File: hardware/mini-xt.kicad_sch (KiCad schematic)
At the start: 0 parts

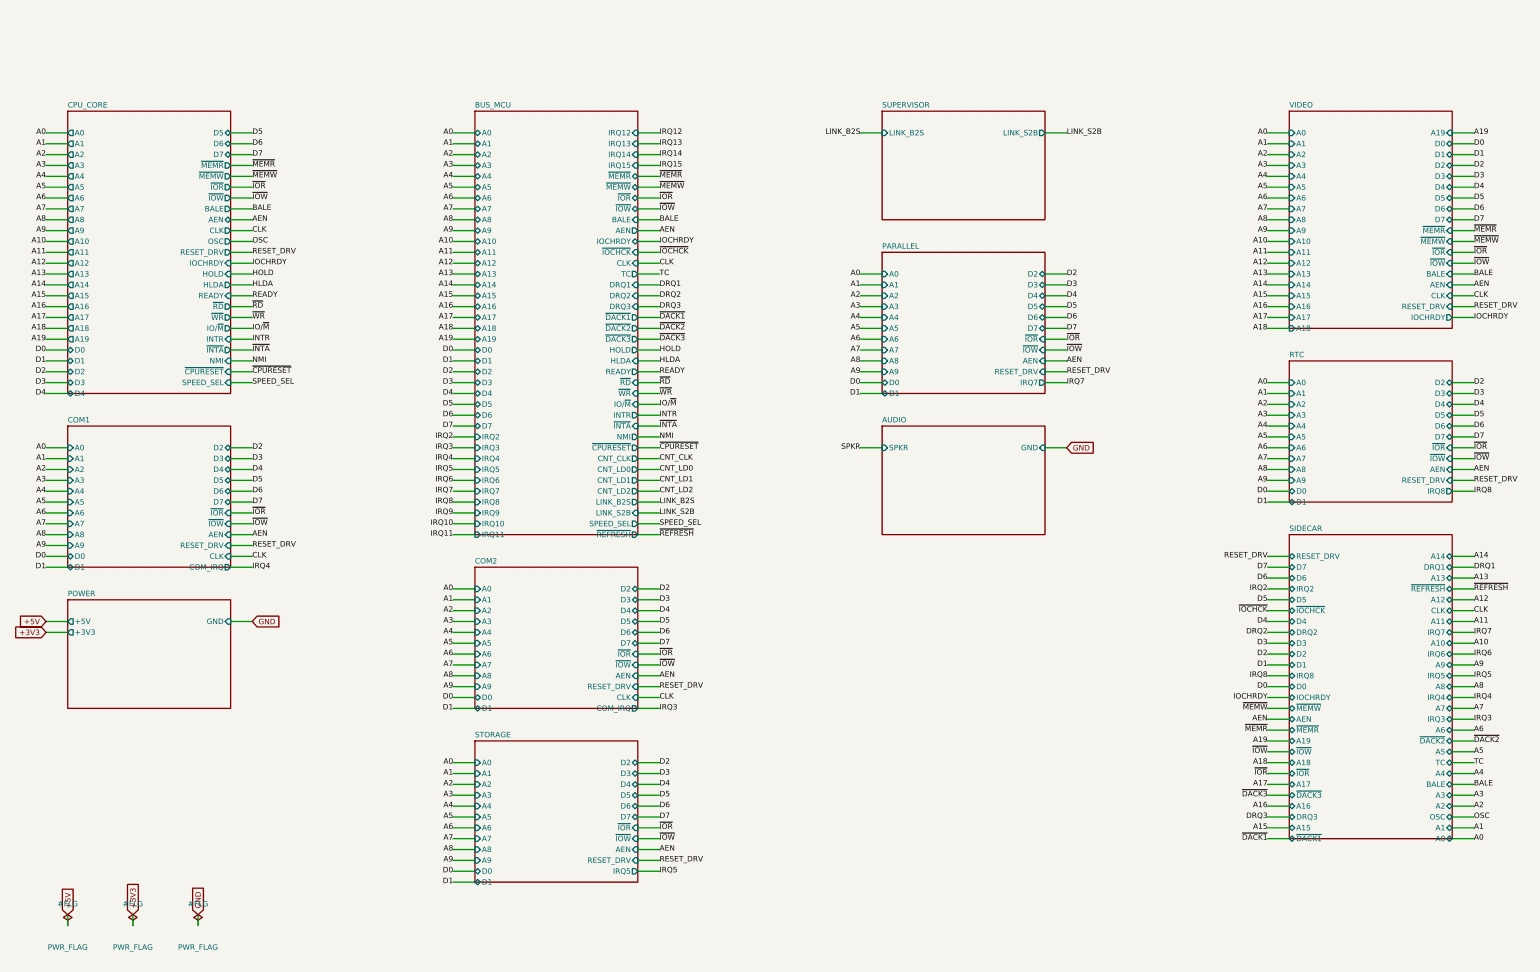
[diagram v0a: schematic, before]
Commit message: Fix all medium design-review findings (M1-M8)
- M1: Supervisor link moved to GPIO4/5 (real UART1 pair); POST -> GPIO6-15
- M2: CNT_RUN = LD0.LD1.LD2 gates every '163 CEP (load-cascade hazard)
- M3: ~WR / IO-M pruned to cpu_core-internal; DRQ2/3 pulled + noted;
  doc S5.2 "as built: 48/48" + S16 updated
- M4: true XT-IDE rev-2 map (A0<->A3 swap): data 0x300, latch 0x301,
  CS1 0x307/0x30F, drive DA0 = bus A3 - matches XTIDE UB "rev 2" type
- M5: COM4 -> bus IRQ2 line (IRQ9 via AT redirect); IRQ10/11/14/15 marked
  off-header; ~REFRESH added to mxbus ISA_CTRL; questions-sidecar superseded
- M6: card_isatest clock tree on unswitched V5RAW (spec S8)
- M7: card_isatest IRQ2-8/DRQ1-3 idle pull-downs (spec S4/S9)
- M8: com_port JP1 selects 16550 RX source (DB9 vs TTL console); 5V note

Rebuilt motherboard + cards; structural ERC = 0; netlist-verified.
Fix log in hardware/notes/design-review-2026-07-03.md (batch 3).

Co-Authored-By: Claude Fable 5 <noreply@anthropic.com>
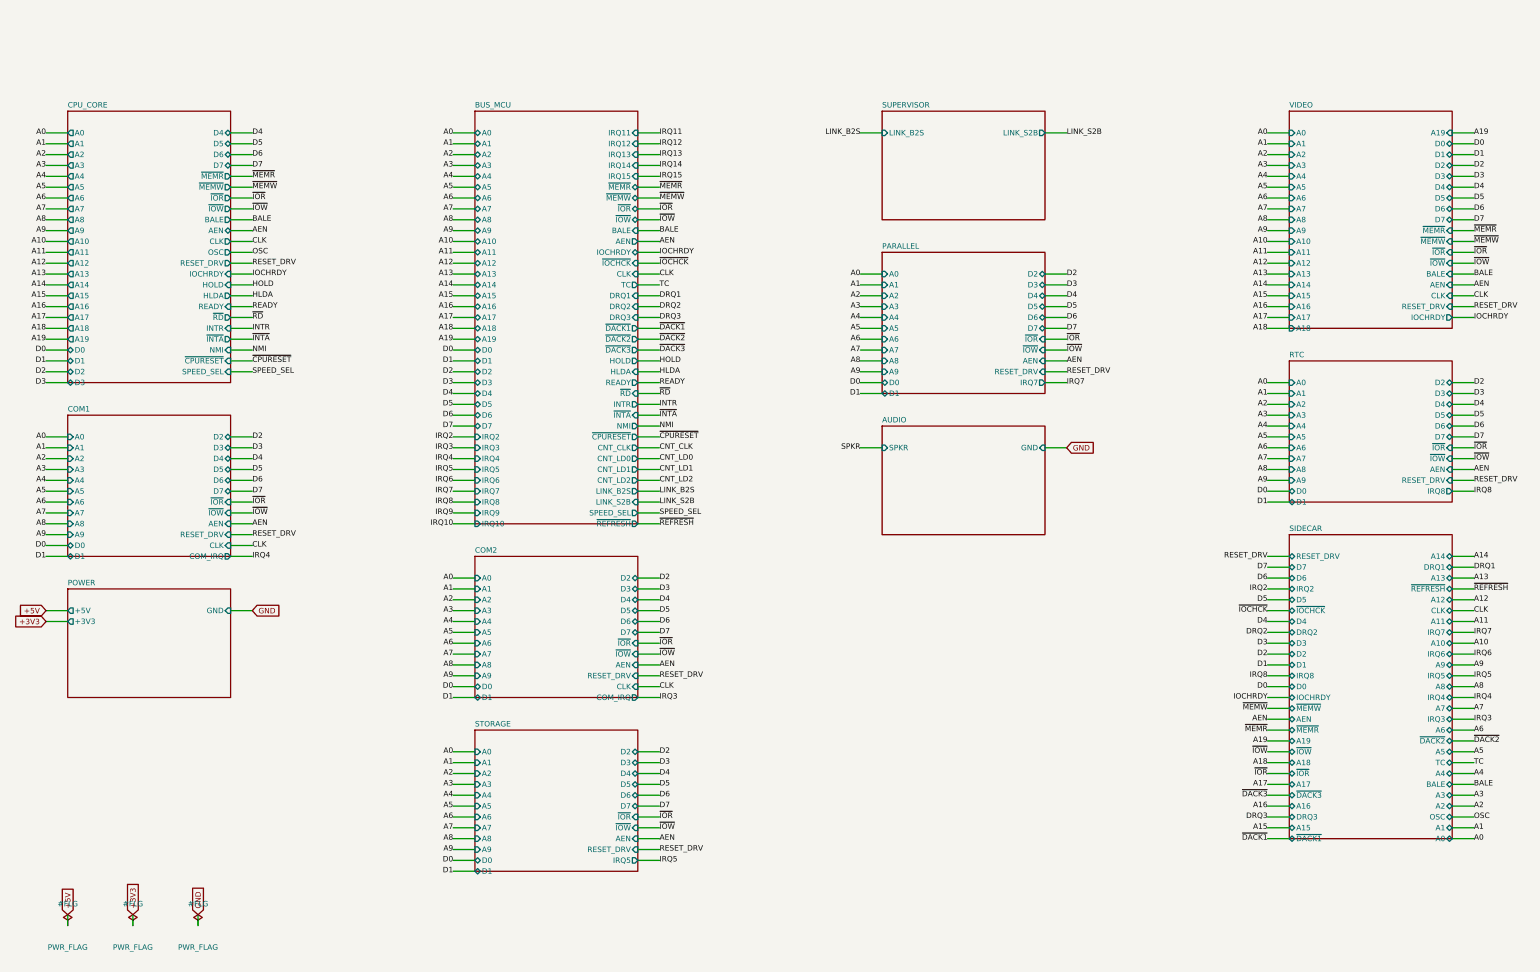
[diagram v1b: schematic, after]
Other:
- sheet BUS_MCU ports: added none; removed IO/~{M}, ~{WR}
- sheet CPU_CORE ports: added none; removed IO/~{M}, ~{WR}

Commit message: Design review 2026-07-11: rail protection, decoupling, wiring fixes
Protection:
- Sidecar +5V now feeds through a 2A polyfuse into +5V_ISA with an
  SMBJ5.0A clamp + 22uF bulk (a faulted ISA card trips its own fuse
  instead of dropping the board; back-fed voltage is clamped).
- USB-C VBUS enters through a 3A polyfuse with an SMBJ5.0A on +5V
  (backstop for the CFG1 9-20V failure mode). CH224K gains a 1uF VDD
  cap; its PG routes to Supervisor GPIO16 as PD_PG. Buck output
  doubled to 2x22uF, 10uF at VIN, extra rail bulk.
- Supervisor USB-A host port: 27R series termination (RP2040
  requirement), USBLC6-2SC6 ESD array, 100uF VBUS bulk.
- Video: HDMI +5V fused (500mA), HPD sensed on GPIO41, 100R series on
  VGA sync. TMDS ESD array deferred to layout (no symbol).
- card_isatest: V5RAW bulk, Q1 gate soft-start cap, TVS on DUT rail.

Wiring fixes:
- SPKR had no driver anywhere (netlist: 1 node). Bus MCU GPIO22
  reassigned from the diagnostics-only bus-CLK sense to SPKR; bus_mcu
  drops CLK from its interface. Doc 5.2 updated.
- bus_mcu C8 decoupled +3V3, a rail that sheet never uses -> 3V3_BUS.
- Storage IRQ5 was push-pull (permanently driven when idle) -> 2N7002
  + gated '125 tri-state, same convention as the LPT IRQ7 stage.
- MAX3241 pump caps resized to the 5V datasheet values (47nF/330nF).
- LPT DB25 status inputs get 4.7k pull-ups (floated with no printer).
- Audio line-out gets a 100R series isolator before the jack.

Best practices:
- Decoupling to ~1x100nF per IC on every sheet + bulk per board
  (cpu_core 7->16 incl. the naked 3.3V oscillator, storage 4->11,
  parallel 6->13, rtc/com/video/bus_mcu/card_isatest similar).
- All floating spare CMOS inputs tied ('00/'74/'157/'02/'04/'125
  sections across cpu_core, bus_mcu, rtc, storage, card_isatest).

Sourcing: new parts mapped in parts.py with JLC-verified LCSC numbers;
Power_Protection lib registered in the tools; TPS563200 stock alert
(4 pcs left at JLC) flagged in parts.py + jlcpcb-sourcing.md. All
decisi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
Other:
- sheet BUS_MCU ports: added SPKR; removed CLK
- sheet POWER ports: added PD_PG; removed none
- sheet SUPERVISOR ports: added PD_PG; removed none
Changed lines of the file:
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@@
 			)
 		)
-		(pin "CLK" input
+		(pin "TC" output
 			(at 158.75 63.5 0)
 			(effects
@@
 			)
 		)
-		(pin "TC" output
+		(pin "DRQ1" input
 			(at 158.75 66.04 0)
 			(effects
@@
 			)
 		)
-		(pin "DRQ1" input
+		(pin "DRQ2" input
 			(at 158.75 68.58 0)
 			(effects
@@
 			)
 		)
-		(pin "DRQ2" input
+		(pin "DRQ3" input
 			(at 158.75 71.12 0)
 			(effects
@@
 			)
 		)
-		(pin "DRQ3" input
+		(pin "~{DACK1}" output
 			(at 158.75 73.66 0)
 			(effects
@@
 			)
 		)
-		(pin "~{DACK1}" output
+		(pin "~{DACK2}" output
 			(at 158.75 76.2 0)
 			(effects
@@
 			)
 		)
-		(pin "~{DACK2}" output
+		(pin "~{DACK3}" output
 			(at 158.75 78.74 0)
 			(effects
@@
 			)
 		)
-		(pin "~{DACK3}" output
+		(pin "HOLD" output
 			(at 158.75 81.28 0)
 			(effects
@@
 			)
 		)
-		(pin "HOLD" output
+		(pin "HLDA" input
 			(at 158.75 83.82 0)
 			(effects
@@
 			)
 		)
-		(pin "HLDA" input
+		(pin "READY" output
 			(at 158.75 86.36 0)
 			(effects
@@
 			)
 		)
-		(pin "READY" output
+		(pin "~{RD}" input
 			(at 158.75 88.9 0)
 			(effects
@@
 			)
 		)
-		(pin "~{RD}" input
+		(pin "INTR" output
 			(at 158.75 91.44 0)
 			(effects
@@
 			)
 		)
-		(pin "INTR" output
+		(pin "~{INTA}" input
 			(at 158.75 93.98 0)
 			(effects
@@
 			)
 		)
-		(pin "~{INTA}" input
+		(pin "NMI" output
 			(at 158.75 96.52 0)
 			(effects
@@
 			)
 		)
-		(pin "NMI" output
+		(pin "~{CPURESET}" output
 			(at 158.75 99.06 0)
 			(effects
@@
 			)
 		)
-		(pin "~{CPURESET}" output
+		(pin "CNT_CLK" output
 			(at 158.75 101.6 0)
 			(effects
@@
 			)
 		)
-		(pin "CNT_CLK" output
+		(pin "CNT_LD0" output
 			(at 158.75 104.14 0)
 			(effects
@@
 			)
 		)
-		(pin "CNT_LD0" output
+		(pin "CNT_LD1" output
 			(at 158.75 106.68 0)
 			(effects
@@
 			)
 		)
-		(pin "CNT_LD1" output
+		(pin "CNT_LD2" output
 			(at 158.75 109.22 0)
 			(effects
@@
 			)
 		)
-		(pin "CNT_LD2" output
+		(pin "LINK_B2S" output
 			(at 158.75 111.76 0)
 			(effects
@@
 			)
 		)
-		(pin "LINK_B2S" output
+		(pin "LINK_S2B" input
 			(at 158.75 114.3 0)
 			(effects
@@
 			)
 		)
-		(pin "LINK_S2B" input
+		(pin "SPEED_SEL" output
 			(at 158.75 116.84 0)
 			(effects
@@
 			)
 		)
-		(pin "SPEED_SEL" output
+		(pin "~{REFRESH}" output
 			(at 158.75 119.38 0)
 			(effects
@@
 			)
 		)
-		(pin "~{REFRESH}" output
+		(pin "SPKR" output
 			(at 158.75 121.92 0)
 			(effects
@@
 		)
 		(pin "LINK_S2B" output
+			(at 215.9 33.02 180)
+			(effects
+				(font
+					(size 1.27 1.27)
+				)
+				(justify right)
+			)
+		)
+		(pin "PD_PG" input
 			(at 254 30.48 0)
 			(effects
@@
 			)
 		)
+		(pin "PD_PG" output
+			(at 63.5 144.78 0)
+			(effects
+				(font
+					(size 1.27 1.27)
+				)
+				(justify left)
+			)
+		)
 		(instances
 			(project "mini-xt"
@@
 		)
 	)
-	(label "CLK"
+	(label "TC"
 		(at 163.83 63.5 0)
 		(effects
@@
 		)
 	)
-	(label "TC"
+	(label "DRQ1"
 		(at 163.83 66.04 0)
 		(effects
@@
 		)
 	)
-	(label "DRQ1"
+	(label "DRQ2"
 		(at 163.83 68.58 0)
 		(effects
@@
 		)
 	)
-	(label "DRQ2"
+	(label "DRQ3"
 		(at 163.83 71.12 0)
 		(effects
@@
 		)
 	)
-	(label "DRQ3"
+	(label "~{DACK1}"
 		(at 163.83 73.66 0)
 		(effects
@@
 		)
 	)
-	(label "~{DACK1}"
+	(label "~{DACK2}"
 		(at 163.83 76.2 0)
 		(effects
@@
 		)
 	)
-	(label "~{DACK2}"
+	(label "~{DACK3}"
 		(at 163.83 78.74 0)
 		(effects
@@
 		)
 	)
-	(label "~{DACK3}"
+	(label "HOLD"
 		(at 163.83 81.28 0)
 		(effects
@@
 		)
 	)
-	(label "HOLD"
+	(label "HLDA"
 		(at 163.83 83.82 0)
 		(effects
@@
 		)
 	)
-	(label "HLDA"
+	(label "READY"
 		(at 163.83 86.36 0)
 		(effects
@@
 		)
 	)
-	(label "READY"
+	(label "~{RD}"
 		(at 163.83 88.9 0)
 		(effects
@@
 		)
 	)
-	(label "~{RD}"
+	(label "INTR"
 		(at 163.83 91.44 0)
 		(effects
@@
 		)
 	)
-	(label "INTR"
+	(label "~{INTA}"
 		(at 163.83 93.98 0)
 		(effects
@@
 		)
 	)
-	(label "~{INTA}"
+	(label "NMI"
 		(at 163.83 96.52 0)
 		(effects
@@
 		)
 	)
-	(label "NMI"
+	(label "~{CPURESET}"
 		(at 163.83 99.06 0)
 		(effects
@@
 		)
 	)
-	(label "~{CPURESET}"
+	(label "CNT_CLK"
 		(at 163.83 101.6 0)
 		(effects
@@
 		)
 	)
-	(label "CNT_CLK"
+	(label "CNT_LD0"
 		(at 163.83 104.14 0)
 		(effects
@@
 		)
 	)
-	(label "CNT_LD0"
+	(label "CNT_LD1"
 		(at 163.83 106.68 0)
 		(effects
@@
 		)
 	)
-	(label "CNT_LD1"
+	(label "CNT_LD2"
 		(at 163.83 109.22 0)
 		(effects
@@
 		)
 	)
-	(label "CNT_LD2"
+	(label "LINK_B2S"
 		(at 163.83 111.76 0)
 		(effects
@@
 		)
 	)
-	(label "LINK_B2S"
+	(label "LINK_S2B"
 		(at 163.83 114.3 0)
 		(effects
@@
 		)
 	)
-	(label "LINK_S2B"
+	(label "SPEED_SEL"
 		(at 163.83 116.84 0)
 		(effects
@@
 		)
 	)
-	(label "SPEED_SEL"
+	(label "~{REFRESH}"
 		(at 163.83 119.38 0)
 		(effects
@@
 		)
 	)
-	(label "~{REFRESH}"
+	(label "SPKR"
 		(at 163.83 121.92 0)
 		(effects
@@
 	(wire
 		(pts
+			(xy 215.9 33.02)
+			(xy 210.82 33.02)
+		)
+		(stroke
+			(width 0)
+			(type default)
+		)
+	)
+	(label "LINK_S2B"
+		(at 210.82 33.02 180)
+		(effects
+			(font
+				(size 1.27 1.27)
+			)
+			(justify right)
+		)
+	)
+	(wire
+		(pts
 			(xy 254 30.48)
 			(xy 259.08 30.48)
@@
 		)
 	)
-	(label "LINK_S2B"
+	(label "PD_PG"
 		(at 259.08 30.48 0)
 		(effects
@@
 		(effects
 			(font
+				(size 1.27 1.27)
+			)
+			(justify left)
+		)
+	)
+	(wire
+		(pts
+			(xy 63.5 144.78)
+			(xy 68.58 144.78)
+		)
+		(stroke
+			(width 0)
+			(type default)
+		)
+	)
+	(label "PD_PG"
+		(at 68.58 144.78 0)
+		(effects
+			(font

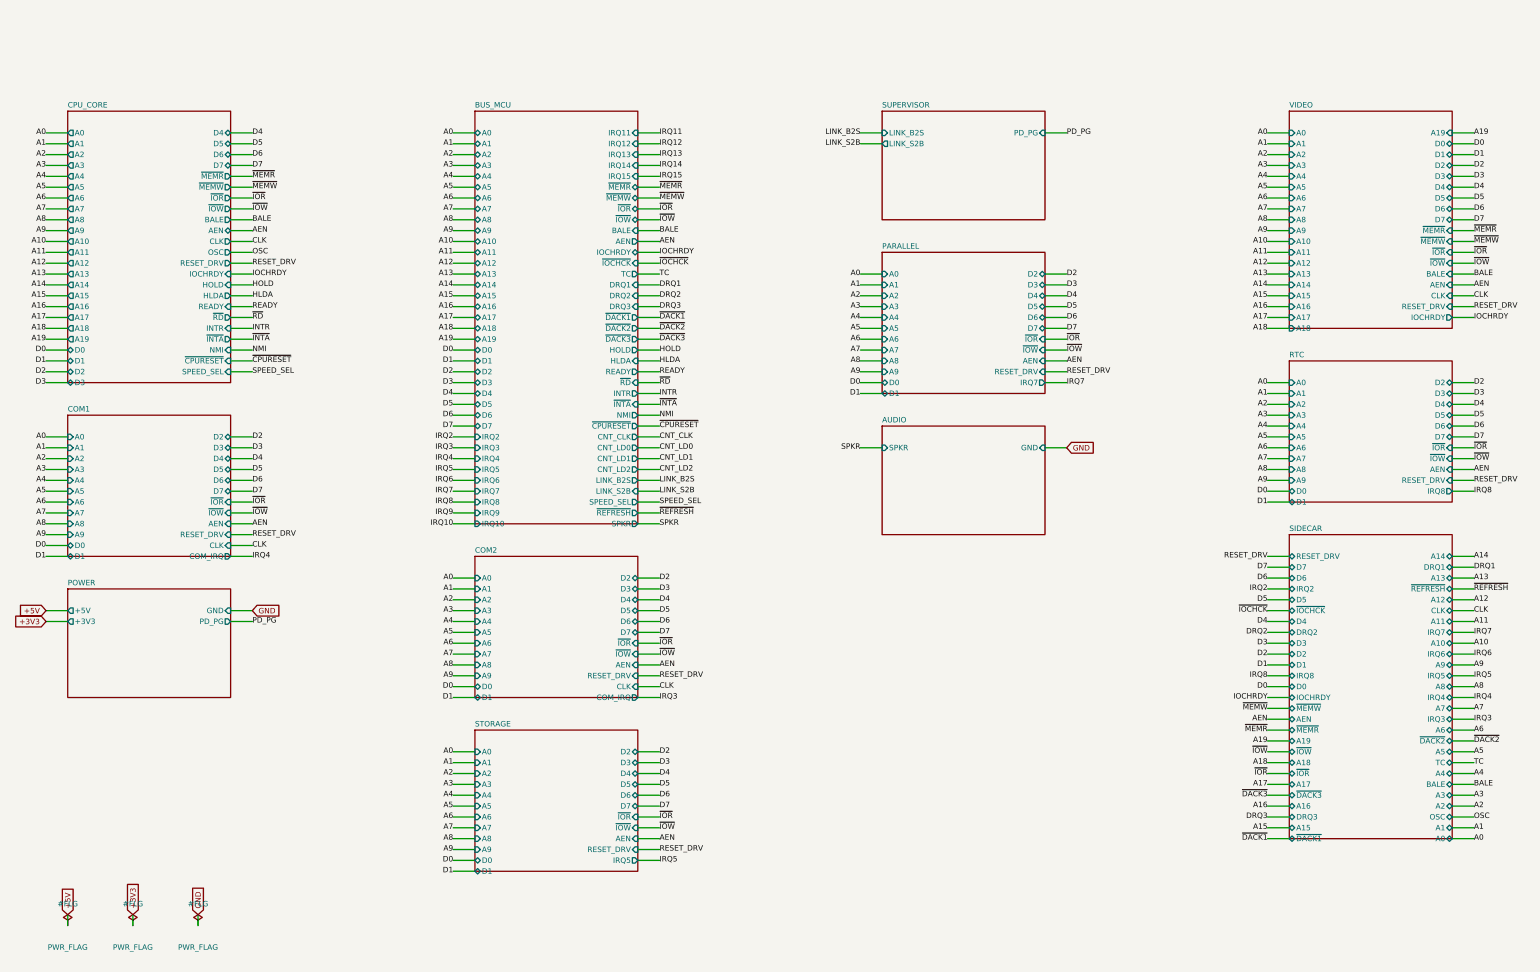
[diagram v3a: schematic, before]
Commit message: COM/LPT: on-board enable jumpers + base-addr/IRQ straps
The motherboard's COM1/COM2 IRQs were hard-wired at build time (INSTANCES
net remap); the LPT port had no strap or disable at all. Both sheets now
carry the full jumper set a real card would have, so an on-board port can
be disabled or re-strapped to make room for the same peripheral on the
sidecar chain:

- com_port: JP3 enable gates the 16550's spare active-high CS1 (open =
  never selected; IRQ needs no gating since MCR resets to 0 -> OUT2# high
  -> '125 released). JP2 picks IRQ4/IRQ3 (open = polled) on the sheet, so
  the sheet now exports IRQ3+IRQ4 and the INSTANCES remap is gone -- both
  instances share the lines safely (tri-state). J2 base strap unchanged.
- parallel: JP1 base 0x378/0x278 (differ only in A8; a spare U12 NAND
  makes ~A8), JP2 enable lifts the register-select '138's spare ~E1 (open
  kills every select, read enable and latch clock), JP3 IRQ7/IRQ5 (open =
  polled; IRQ5 noted as conflicting with the storage card if both enabled).
  PINS now export IRQ5+IRQ7.
- parts.py: Conn_01x02 breakaway-header fallback for the 2-pin jumpers.

Downstream sheet .kicad_sch diffs are instance-path UUID shifts from the
grown com_port/parallel interfaces (deterministic counter), not edits.

Verified: netlist shows IRQ3/IRQ4 spanning sidecar + both COM straps + the
Bus MCU collector; IRQ5 spans sidecar + LPT strap + storage + collector;
each enable net ties jumper + pull resistor + chip-select pin. Zero
structural ERC on motherboard and cards.

Co-Authored-By: Claude Fable 5 <noreply@anthropic.com>
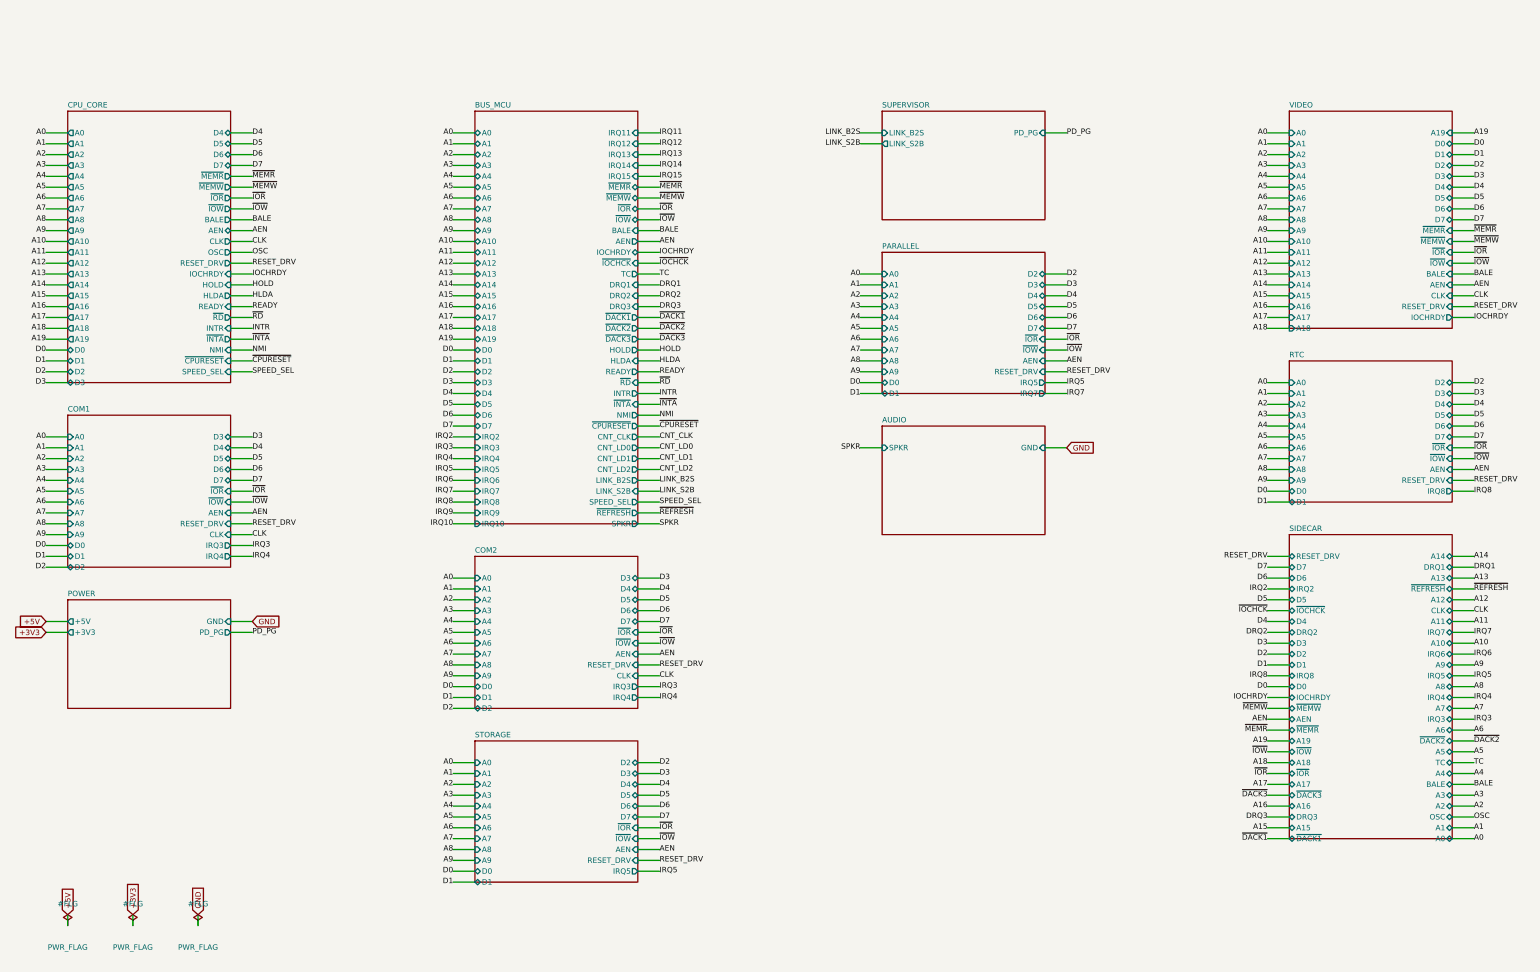
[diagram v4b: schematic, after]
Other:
- sheet COM1 ports: added IRQ3, IRQ4; removed COM_IRQ
- sheet COM2 ports: added IRQ3, IRQ4; removed COM_IRQ
- sheet PARALLEL ports: added IRQ5; removed none
